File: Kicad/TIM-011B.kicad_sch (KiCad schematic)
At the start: 63 parts, among them P2 POWER, P3 EXPAND, P5 POWER

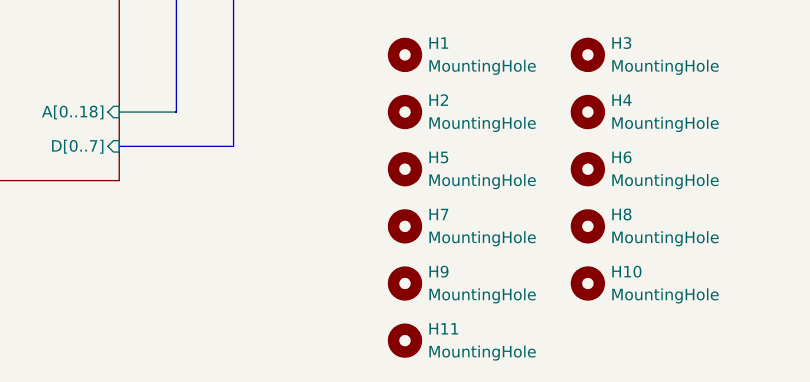
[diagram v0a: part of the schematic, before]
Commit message: U18 correction, ROM A13 ground, DB25 mouting hole fix, remove H9, Credits Update
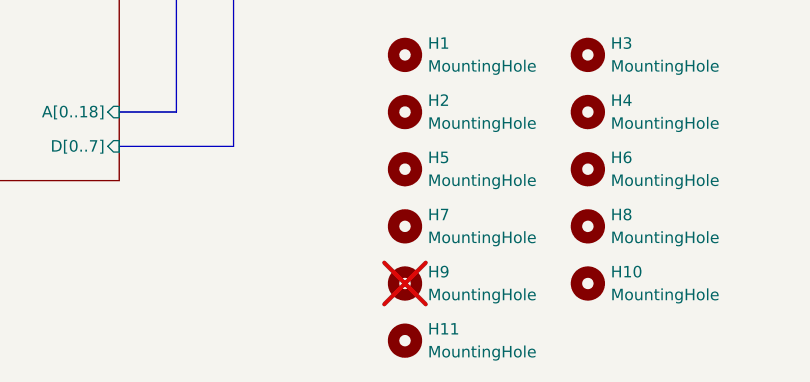
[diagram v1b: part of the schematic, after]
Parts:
- H9: now not fitted
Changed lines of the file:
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@@
 		(exclude_from_sim yes)
 		(in_bom no)
-		(on_board yes)
-		(dnp no)
+		(on_board no)
+		(dnp yes)
 		(fields_autoplaced yes)
 		(property "Reference" "H9"
